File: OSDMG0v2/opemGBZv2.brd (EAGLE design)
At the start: 81.3 x 69.4 mm, 62 parts, among them IC2 TP4056, J1 SJ2-35954D-SMT-TR, T1 BC846S, U3 FS312F-G, U4 FS8205

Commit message: update board
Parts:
- removed JP2: (no value), pinhead:1X13
- removed U4: FS8205, fs8205:SOT23-6
- added C11, C12: 18pF, adafruit:C0805K
- added C13, C14, C4, C5: 0.1uF, adafruit:C0805K
- added C6: 10uF, adafruit:A/3216-18R
- added IC1: ATMEGA32U4-AU, adaprog:TQFP44
- added JP3, JP4: (no value), pinhead:1X02
- added PWR: GREEN, adafruit:CHIPLED_0805
- added R18, R7: 22, rcl:R0603
- added R19: 1k, rcl:R0603
- added RPI-D+, RPI-D-: (no value), wirepad:SMD1,27-2,54
- added S2: JS202011SCQN, JS202011SCQN:SW_JS202011SCQN
- added SJ2: VCC, jumper:SJ
- added U1: FS8205, fs8205:SOT23-6
- added X3: 16MHz, adaprog:NX5032
- moved RESET 346.4 mm to (80.5, 51.4), flipped to the bottom, turned to 270 degrees
- moved C3 343.9 mm to (75.6, 62.6), flipped to the bottom, turned to 90 degrees
- moved 12K 334.2 mm to (67.7, 59.9), flipped to the bottom, turned to 270 degrees
- moved 23K 327.5 mm to (71.7, 53.2), flipped to the bottom, turned to 270 degrees
- moved R5 323.8 mm to (69.7, 59.9), flipped to the bottom, turned to 90 degrees
- moved R6 322.5 mm to (69.7, 53.2), flipped to the bottom, turned to 270 degrees
- moved JP1 319.0 mm to (7.99, 63.5)
- moved R1 317.5 mm to (71.7, 59.9), flipped to the bottom, turned to 90 degrees
- moved R4 317.2 mm to (61.4, 62.8), flipped to the bottom
- moved GND-B 315.3 mm to (14.5, 63.7), flipped to the bottom, turned to 180 degrees
- moved 5V-B 314.7 mm to (16.6, 63.8), flipped to the bottom, turned to 180 degrees
- moved T1 311.0 mm to (69.7, 56.6), flipped to the bottom
- moved MMBT9015C 300.5 mm to (61.6, 59.1), flipped to the bottom, turned to 270 degrees
- moved BF998E6327HTSA1 288.6 mm to (61.9, 52.8), flipped to the bottom, turned to 90 degrees
- moved SW2 270.5 mm to (80.5, 53.8), flipped to the bottom, turned to 270 degrees
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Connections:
- removed net N$10: JP2.11, Y.P$2
- removed net N$3: DOWN.P$2, JP2.4
- removed net N$4: JP2.5, RIGHT.P$2
- removed net N$5: JP2.6, SELECT.P$1
- removed net N$6: JP2.7, START.P$1
- removed net N$7: B.P$2, JP2.8
- removed net N$8: A.P$2, JP2.9
- removed net N$9: JP2.10, X.P$2
- new net +3V3: C4.1, IC1.6
- new net A0/D18: IC1.36, START.P$1
- new net A1/D19: IC1.37, SELECT.P$1
- new net A11/D12: IC1.26
- new net A2/D20: IC1.38
- new net A3/D21: IC1.39
- new net A4/D22: IC1.40
- new net A5/D23: IC1.41
- new net A6/D4: IC1.25
- new net A7/D6: IC1.27, JP3.2
- new net AREF: IC1.42
- new net AT-D+: R18.2, S2.2
- new net AT-D-: R7.2, S2.5
- new net D+: S2.1, USBC1.A6, USBC1.B6
- new net D-: S2.4, USBC1.A7, USBC1.B7
- new net D0: IC1.20
- new net D1: IC1.21
- new net D10/A10: IC1.30
- new net D11: IC1.12
- new net D13: IC1.32
- new net D14: A.P$2, IC1.11
- new net D15: IC1.9
- new net D16: B.P$2, IC1.10
- new net D17: IC1.8
- new net D2: IC1.19, UP.P$2
- new net D3: IC1.18, LEFT.P$2
- new net D4: DOWN.P$2
- new net D5: IC1.31, RIGHT.P$2
- new net D7: IC1.1, JP3.1
- new net D8/A8: IC1.28, Y.P$2
- new net D9/A10: IC1.29, X.P$2
- new net N$41: IC1.3, R7.1
- new net N$42: IC1.4, R18.1
- new net N$43: C12.1, IC1.16, X3.P$1
- new net N$44: C11.1, IC1.17, X3.P$2
- new net N$45: PWR.A, R19.2
- net 5V: now also C5.1, C6.+, IC1.2, IC1.7, R19.1, SJ2.2
- net BAT-: now also U1.6; no longer U4.1
- net GND: now also C11.2, C12.2, C13.2, C14.2, C4.2, C5.2, C6.-, IC1.15, IC1.23, IC1.35, IC1.43, IC1.5, PWR.C, U1.4; no longer JP2.1, U4.3
- net L-OUT: now also JP4.1; no longer JP2.12
- net N$1: now also RPI-D-.1, S2.6; no longer JP2.2, LEFT.P$2
- net N$2: now also RPI-D+.1, S2.3; no longer JP2.3, UP.P$2
- net N$37: now also U1.3; no longer U4.4
- net N$38: now also U1.1; no longer U4.6
- net R-OUT: now also JP4.2; no longer JP2.13
- net VCC: now also C13.1, C14.1, IC1.14, IC1.24, IC1.34, IC1.44, SJ2.1
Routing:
- net 5V: track 0.00 -> 202.5 mm, vias 0 -> 5
- net D-: track 0.00 -> 106.9 mm, vias 0 -> 3
- net N$28: track 0.00 -> 97.5 mm, vias 0 -> 4
- net N$22: track 0.00 -> 97.2 mm, vias 0 -> 4
- net BAT+: track 0.00 -> 93.3 mm
- net N$29: track 0.00 -> 80.3 mm, vias 0 -> 4
- net D+: track 0.00 -> 67.9 mm, vias 0 -> 4
- net VCC: track 0.00 -> 64.5 mm
- net N$23: track 0.00 -> 60.3 mm, vias 0 -> 2
- net N$26: track 0.00 -> 59.1 mm, vias 0 -> 4
- net N$24: track 0.00 -> 59.1 mm, vias 0 -> 4
- net N$11: track 0.00 -> 51.6 mm, vias 0 -> 2
- net N$33: track 0.00 -> 51.3 mm, vias 0 -> 2
- net VBUS: track 0.00 -> 48.8 mm
- net R-OUT: track 0.00 -> 46.0 mm, vias 0 -> 1
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- added copper zone on layer 1, net GND
- added copper zone on layer 16, net GND
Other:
- board text removed: "+"
- board text removed: "A"
- board text removed: "B"
- board text removed: "DOWN"
- board text removed: "GND"
- board text removed: "LEFT"
- board text removed: "RIGHT"
- board text removed: "SELECT"
- board text removed: "START"
- board text removed: "UP"
- board text removed: "X"
- board text removed: "Y"

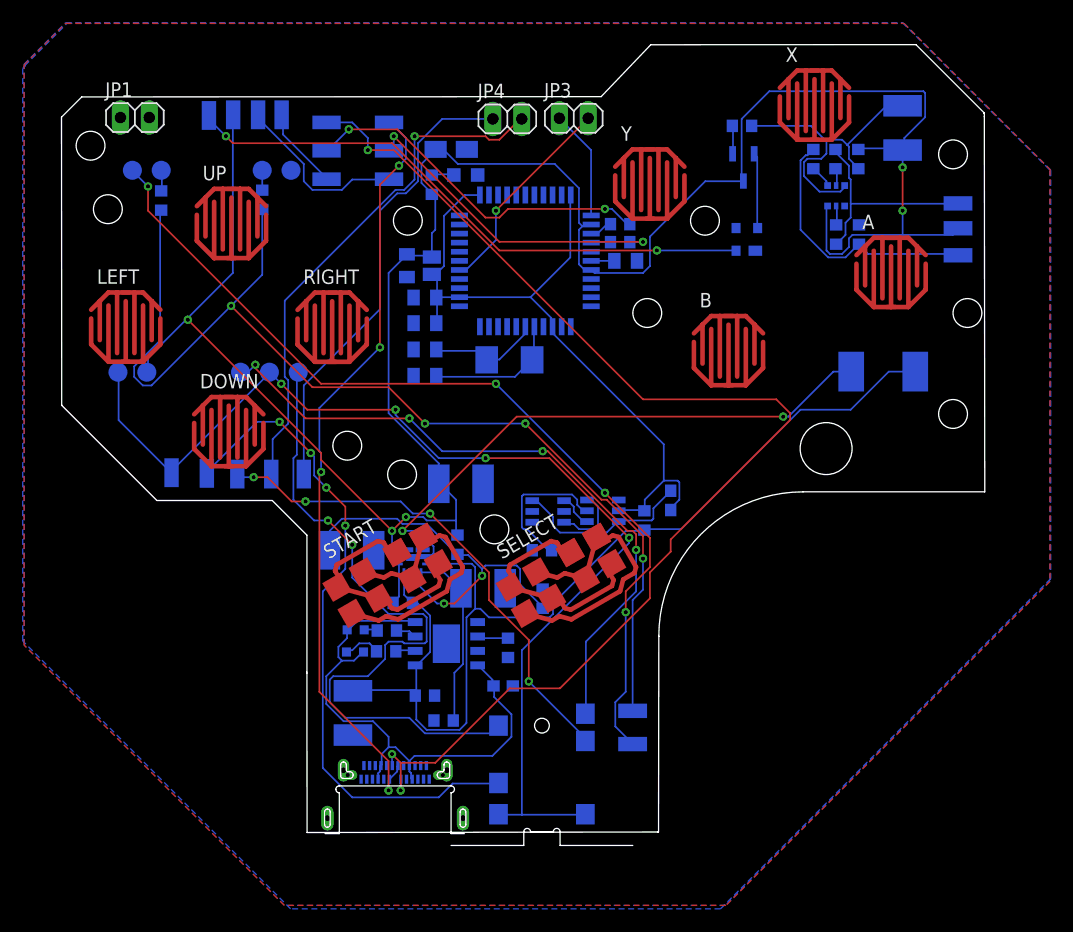
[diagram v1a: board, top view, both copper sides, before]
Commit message: everything routed up GND
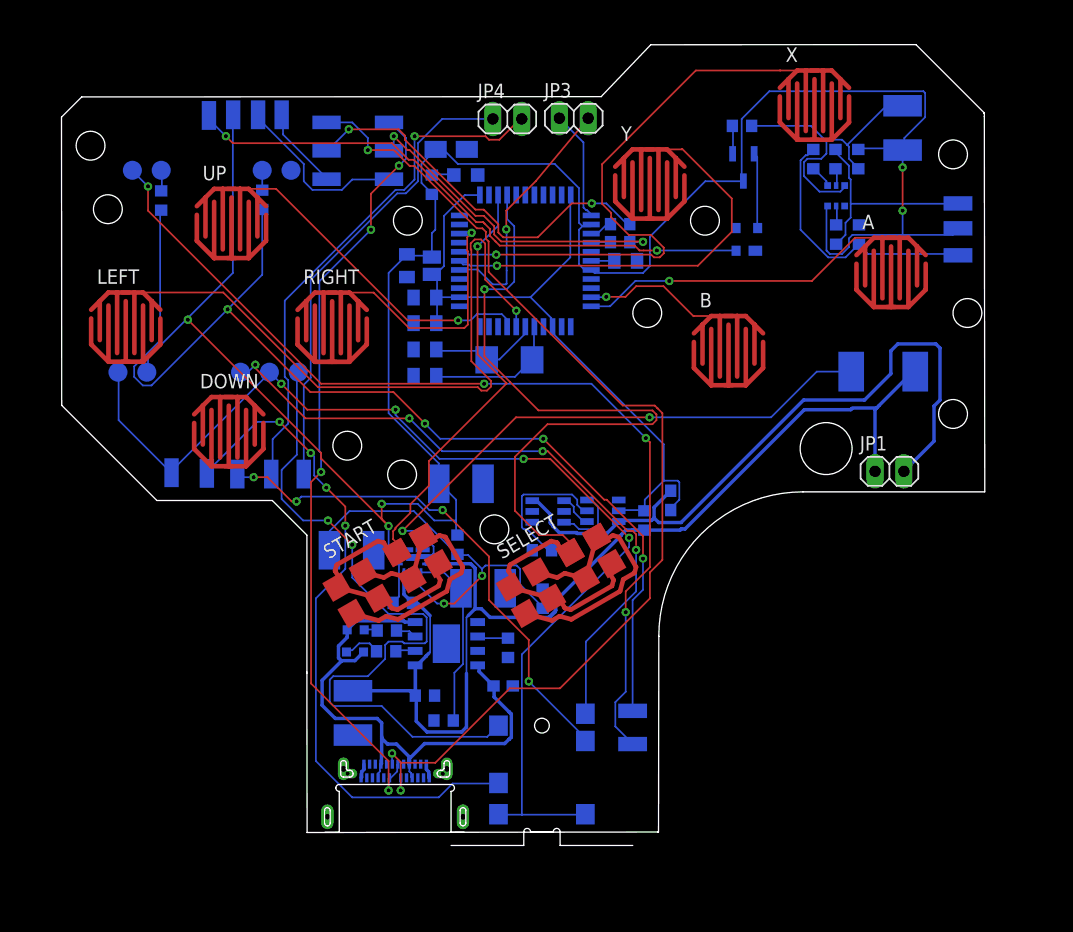
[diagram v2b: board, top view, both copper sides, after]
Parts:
- moved JP1 73.4 mm to (74.4, 32.4)
- moved USBC1 0.12 mm to (30.9, 1.95)
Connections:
- net BAT+: now also JP1.1
- net BAT-: now also JP1.2
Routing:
- net A1/D19: track 0.00 -> 59.9 mm, vias 0 -> 1
- net D3: track 0.00 -> 59.3 mm, vias 0 -> 1
- net D9/A10: track 0.00 -> 51.7 mm, vias 0 -> 1
- net BAT-: track 15.9 -> 61.4 mm
- net A0/D18: track 0.00 -> 37.6 mm, vias 0 -> 1
- net D8/A8: track 0.00 -> 37.4 mm, vias 0 -> 1
- net D2: track 0.00 -> 30.1 mm, vias 0 -> 1
- net D14: track 0.00 -> 29.0 mm, vias 0 -> 1
- net D5: track 0.00 -> 22.7 mm, vias 0 -> 1
- net BAT+: track 93.3 -> 115.4 mm
- net D-: track 106.9 -> 93.1 mm
- net D16: track 0.00 -> 13.6 mm, vias 0 -> 1
- net VBUS: track 48.8 -> 58.2 mm
- net N$29: track 80.3 -> 85.2 mm
- net A7/D6: track 18.4 -> 22.1 mm
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- removed copper zone on layer 1, net GND
- removed copper zone on layer 16, net GND
